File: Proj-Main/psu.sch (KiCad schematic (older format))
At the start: 114 parts, among them J1 METER, J3 T1A, J4 T1B, J5 T1C, J6 SENSE, J8 OUT+, J9 OUT-, Q1 BC856, Q10 MMBT2907A, Q11 PMP4201Y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

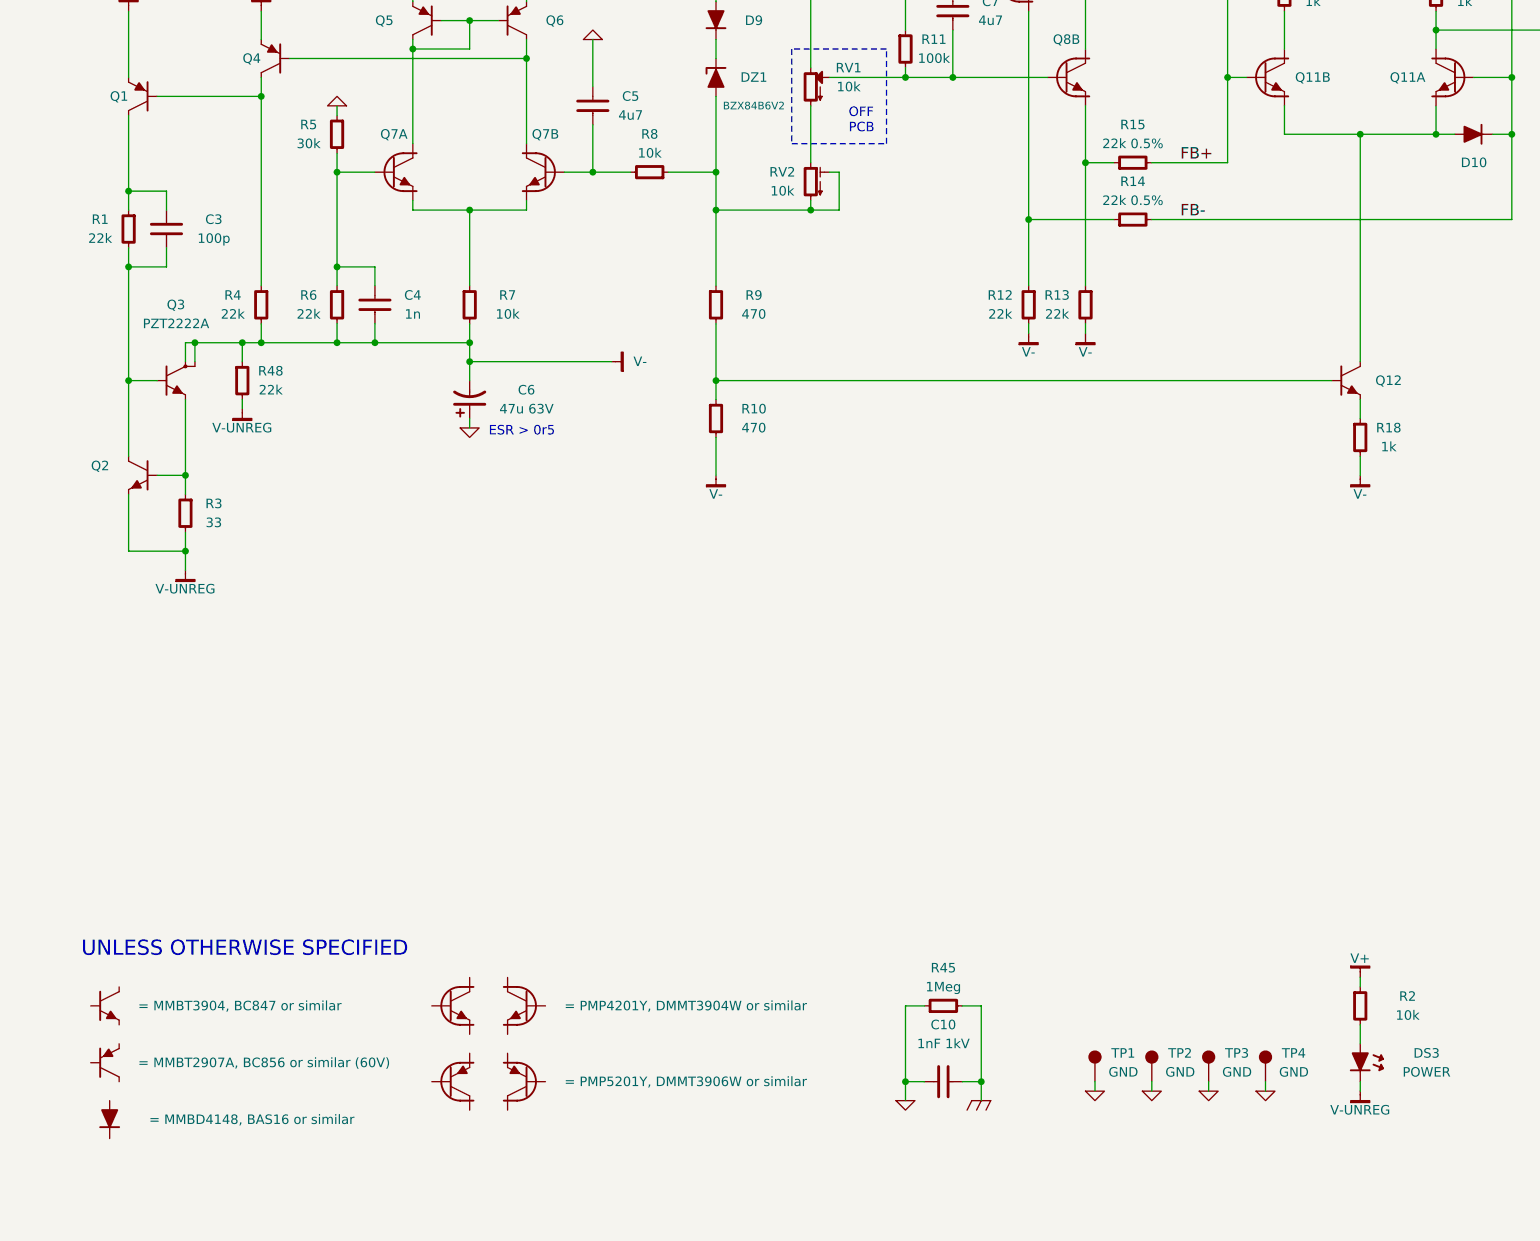
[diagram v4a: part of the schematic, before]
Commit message: Improved design of current source
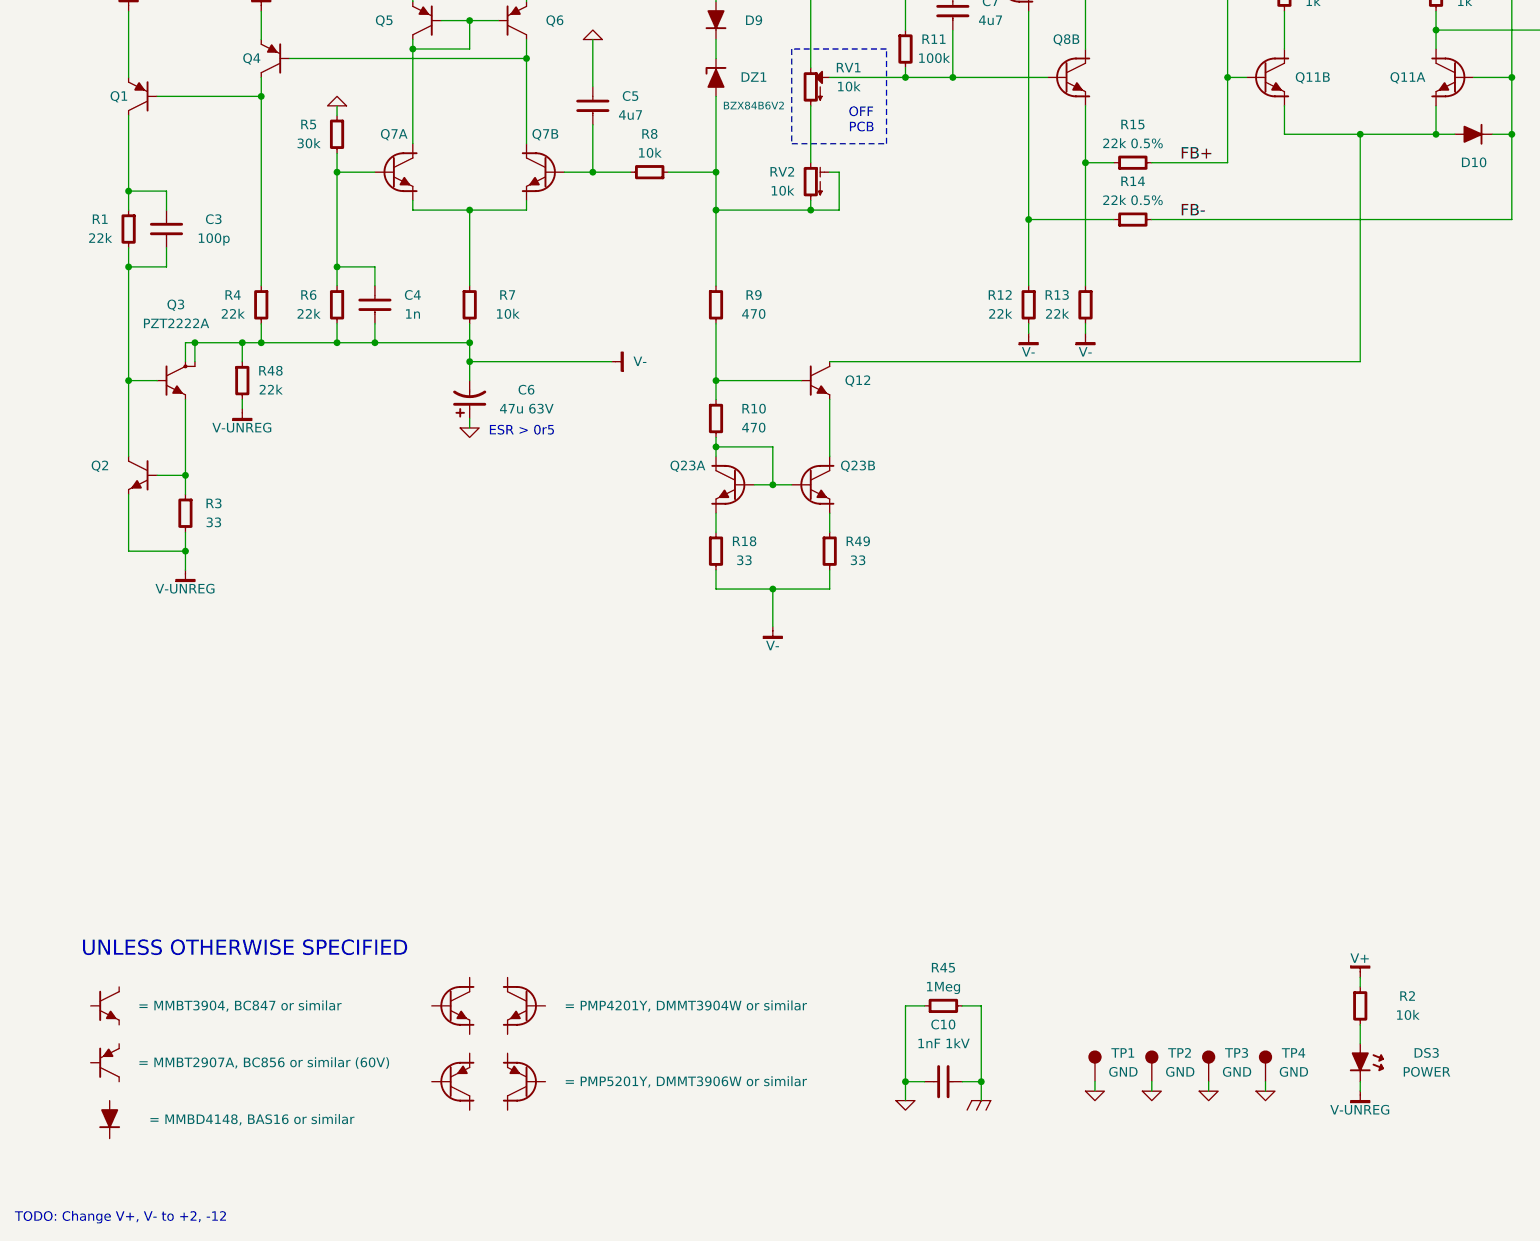
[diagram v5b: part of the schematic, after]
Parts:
- added Q23: PMP4201Y, symbol PMP4201Y
- added R49: 33, symbol R-0805
- R18: value 1k -> 33
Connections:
- net V-: now also R49.2; no longer R10.2
- net at Q12.2: now also Q23.3; no longer R18.1
- new net: Q23.5, R18.1
- new net: Q23.1, Q23.2, Q23.6, R10.2
- new net: Q23.4, R49.1
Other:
- note added: "TODO: Change V+, V- to +2, -12"
- moved on the sheet: Q12, R18

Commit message: Added new thermal cutoff
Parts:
- removed Q10, Q13, Q9: MMBT2907A, symbol MMBT2907A
- added DZ3: 3v0, symbol BZX84C
- added Q10, Q13, Q9: BC856, symbol BC856
- added Q24: MMBT3904, symbol MMBT3904
- added R50: 1k, symbol R-0805
- added R51, R52, R53: 10k, symbol R-0805
- R42: value 100k -> 10k
- R43: value 100k -> NTC; Option NTC -> (none); PartNo NTCLE100E3104JB0 -> NTCLE100E3334JB0
- R44: value 270 -> 1k
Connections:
- net FB-: now also Q24.3; no longer R41.1, R42.1
- net GND: now also C9.1, Q21.2, R44.1; no longer R43.1
- net V+: now also Q10.2, Q9.2
- net V-: now also R43.1, Q24.2, R51.2, R52.2; no longer C9.2, R44.2
- net at Q11.6, R17.2: now also Q13.1
- net at R19.2: now also Q13.2
- net at Q14.1, R20.1: now also Q13.3
- net at R17.1: now also Q10.3
- net at Q22.3, R42.2: now also C9.2, R43.2, R50.2; no longer Q21.1
- net at R41.2: now also Q22.1; no longer DS2.A
- net at DS2.K: now also R41.1, DZ3.1, R51.1, R52.1, R53.2; no longer Q21.2
- net at R16.1: now also Q10.1, Q9.1, Q9.3
- new net: Q21.1, R42.1
- new net: R44.2, R50.1
- new net: DS2.A, DZ3.3, Q21.3
- new net: Q24.1, R53.1
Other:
- moved on the sheet: C9, DS2, Q21, Q22, R41, R42, R43, R44

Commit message: Added current mirror degeneration resistors R54, R55
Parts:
- added R54, R55: 100, symbol R-0805
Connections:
- net V+: now also R54.1, R55.1; no longer Q10.2, Q9.2
- new net: Q9.2, R54.2
- new net: Q10.2, R55.2

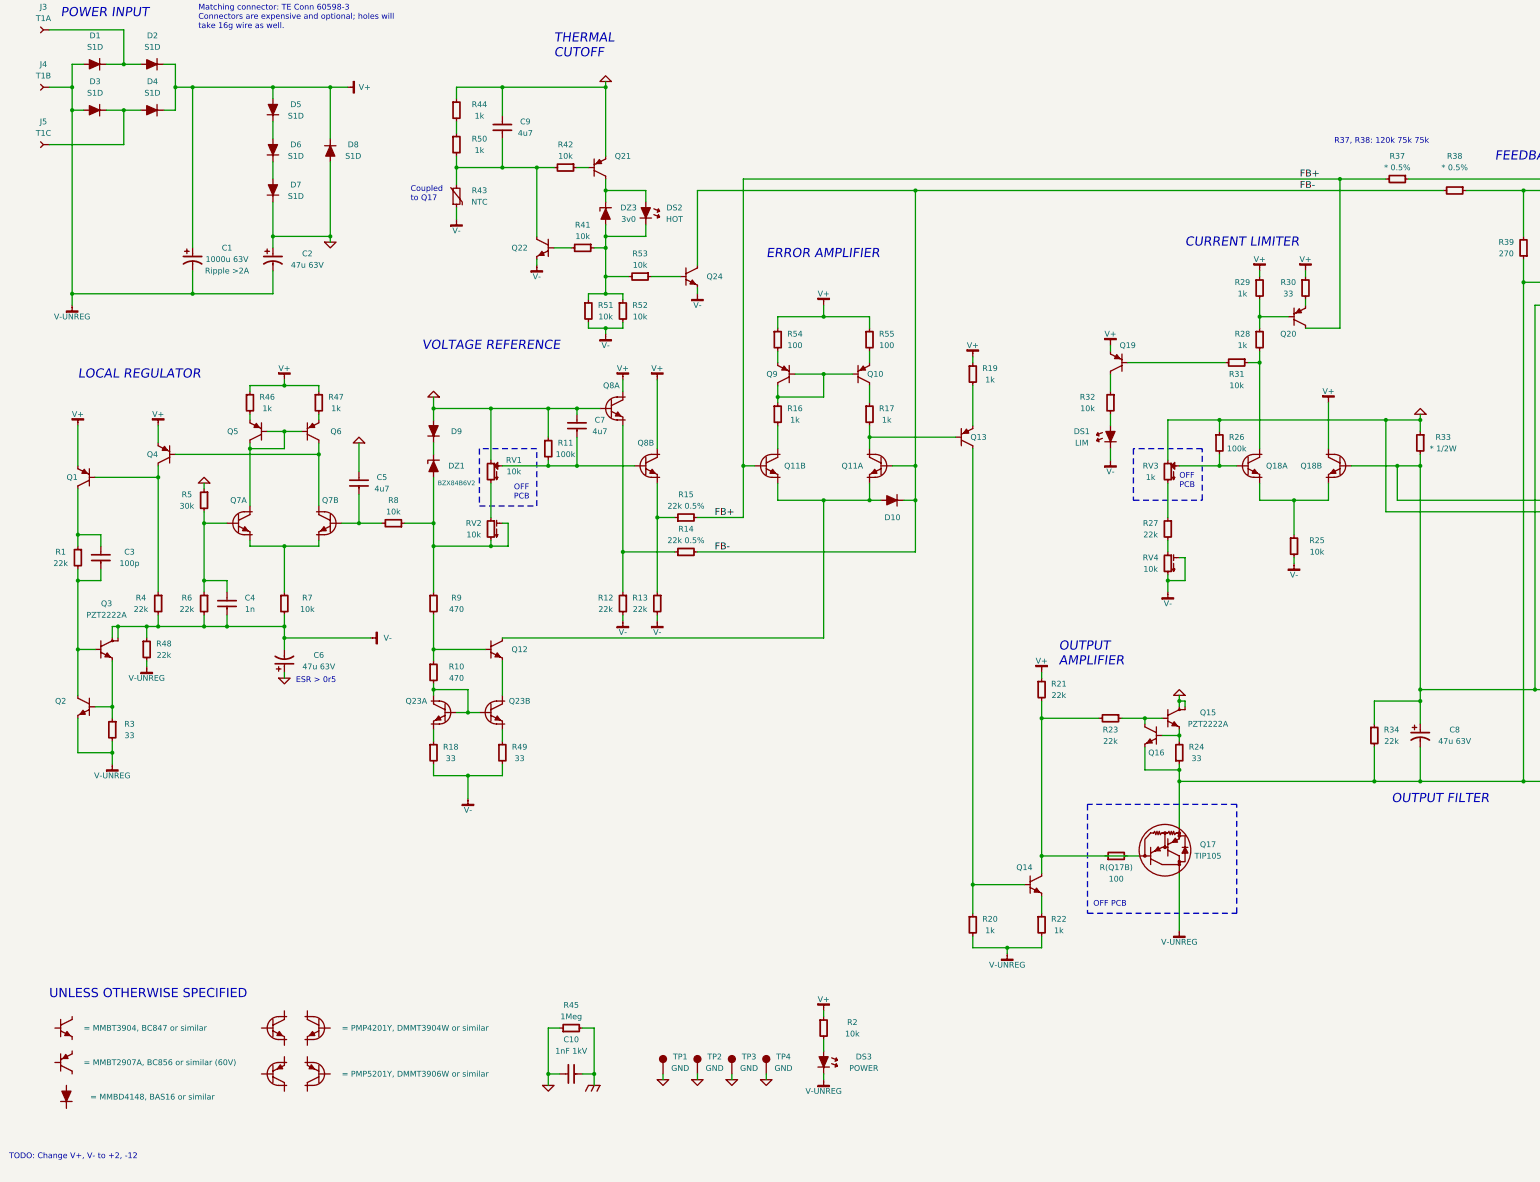
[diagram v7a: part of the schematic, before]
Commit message: Renamed voltage rails (V+ and V- now +2 and -12)
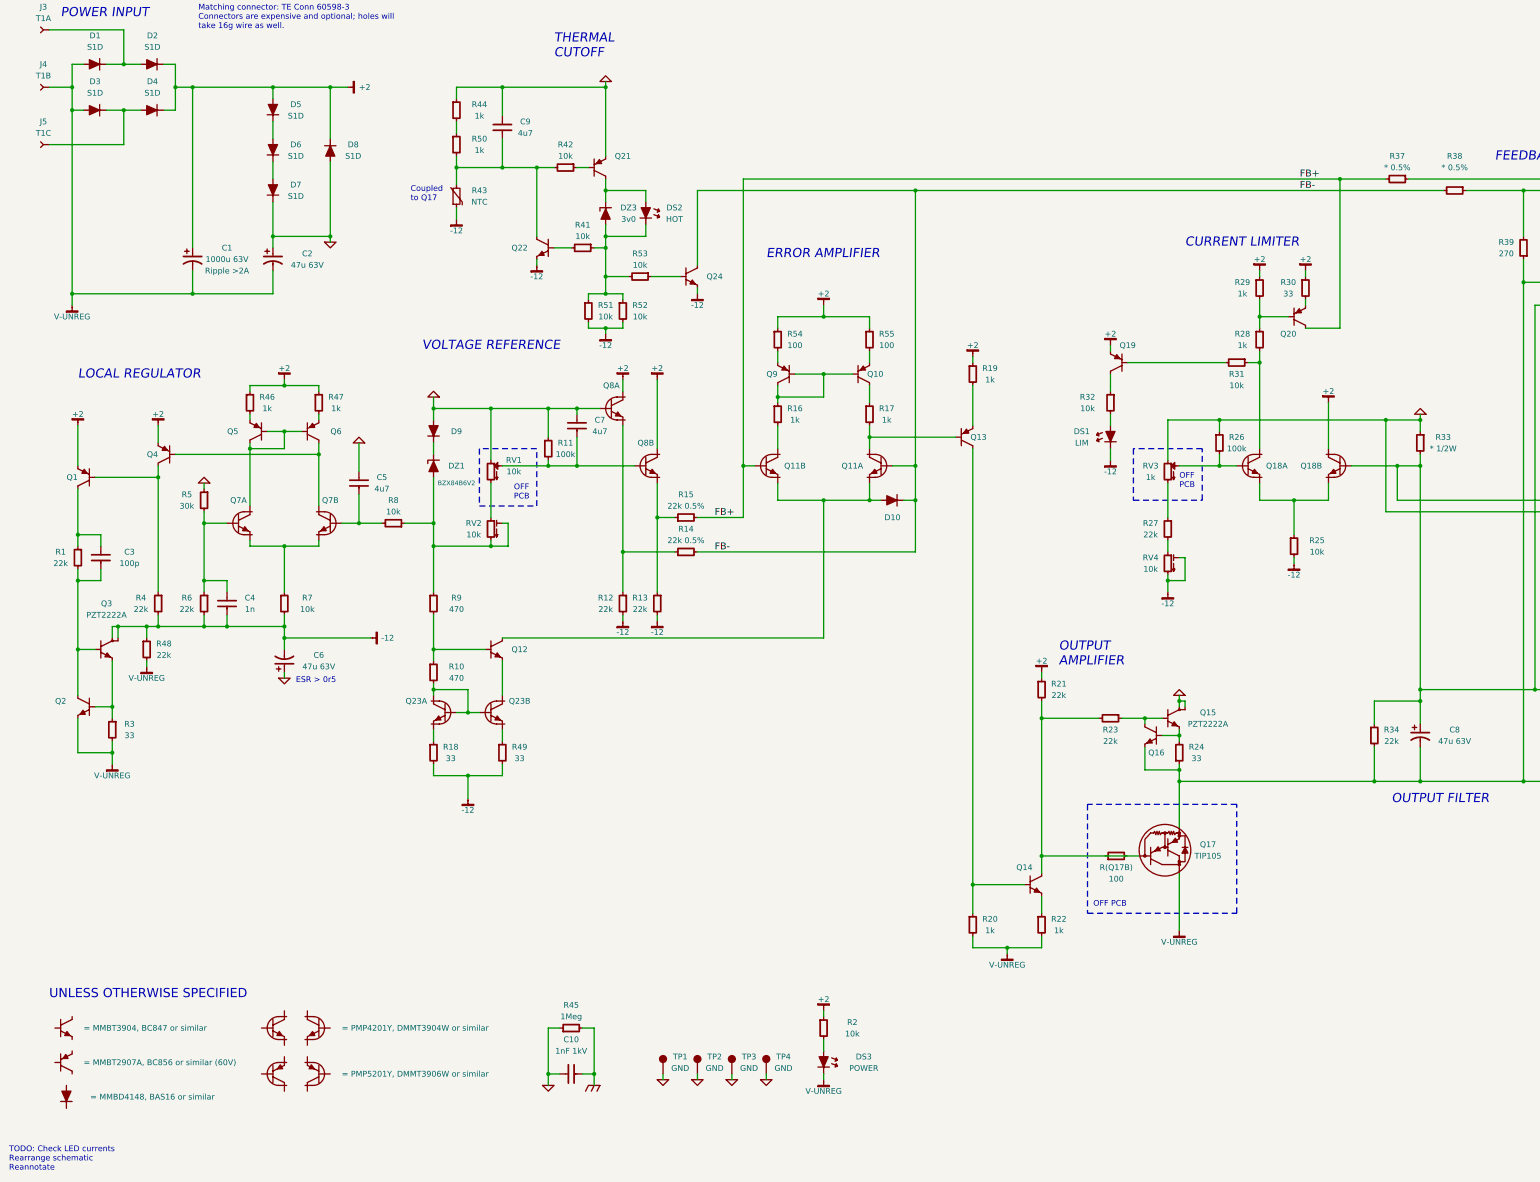
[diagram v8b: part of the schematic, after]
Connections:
- net V+ renamed +2
- net V- renamed -12
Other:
- note added: "TODO: Check LED currents\nRearrange schematic\nReannotate"
- note removed: "R37, R38: 120k 75k 75k"
- note removed: "TODO: Change V+, V- to +2, -12"
